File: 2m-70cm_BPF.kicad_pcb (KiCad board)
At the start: 2 copper layers, 68.2 x 24 mm, 18 parts, among them J1 Conn_Coaxial, J2 Conn_Coaxial

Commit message: Adjusted dividers masks.
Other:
- board text added: "3-POLE CHEBYSHEV BAND-PASS FILTER R1 Max. 37dBM - 5W"
- board text removed: "3-POLE CHEBYSHEV BAND-PASS FILTER R1"
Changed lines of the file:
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@@
 		(layer "Edge.Cuts")
 	)
-	(gr_text "3-POLE CHEBYSHEV \nBAND-PASS FILTER R1"
-		(at 126 129 0)
+	(gr_text "3-POLE CHEBYSHEV \nBAND-PASS FILTER R1\nMax. 37dBM - 5W"
+		(at 125.1 129.8 0)
 		(layer "F.Mask")
 		(effects
@@
 			)
 		)
+	)
+	(zone
+		(net 0)
+		(net_name "")
+		(layer "B.Mask")
+		(hatch edge 0.5)
+		(connect_pads yes
+			(clearance 0.3)
+		)
+		(min_thickness 0.25)
+		(filled_areas_thickness no)
+		(fill yes
+			(thermal_gap 0.5)
+			(thermal_bridge_width 0.5)
+		)
+		(polygon
+			(pts
+				(xy 109.3 132.5) (xy 107.7 132.2) (xy 109.5 123.6) (xy 111.1 123.9)
+			)
+		)
+	)
+	(zone
+		(net 0)
+		(net_name "")
+		(layer "B.Mask")
+		(hatch edge 0.5)
+		(connect_pads yes
+			(clearance 0.3)
+		)
+		(min_thickness 0.25)
+		(filled_areas_thickness no)
+		(fill yes
+			(thermal_gap 0.5)
+			(thermal_bridge_width 0.5)
+		)
+		(polygon
+			(pts
+				(xy 123.600001 147.9) (xy 121.989736 147.9) (xy 121.989737 123.9) (xy 123.6 123.9)
+			)
+		)
+	)
+	(zone
+		(net 0)
+		(net_name "")
+		(layer "B.Mask")
+		(hatch edge 0.5)
+		(connect_pads yes
+			(clearance 0.3)
+		)
+		(min_thickness 0.25)
+		(filled_areas_thickness no)
+		(fill yes
+			(thermal_gap 0.5)
+			(thermal_bridge_width 0.5)
+		)
+		(polygon
+			(pts
+				(xy 107.7 132.2) (xy 109.3 132.5) (xy 106.4 134.7) (xy 104.8 134.4)
+			)
+		)
+	)
+	(zone
+		(net 0)
+		(net_name "")
+		(layer "B.Mask")
+		(hatch edge 0.5)
+		(connect_pads yes
+			(clearance 0.3)
+		)
+		(min_thickness 0.25)
+		(filled_areas_thickness no)
+		(fill yes
+			(thermal_gap 0.5)
+			(thermal_bridge_width 0.5)
+		)
+		(polygon
+			(pts
+				(xy 104.5 148.3) (xy 102.9 147.9) (xy 104.8 134.4) (xy 106.4 134.7)
+			)
+		)

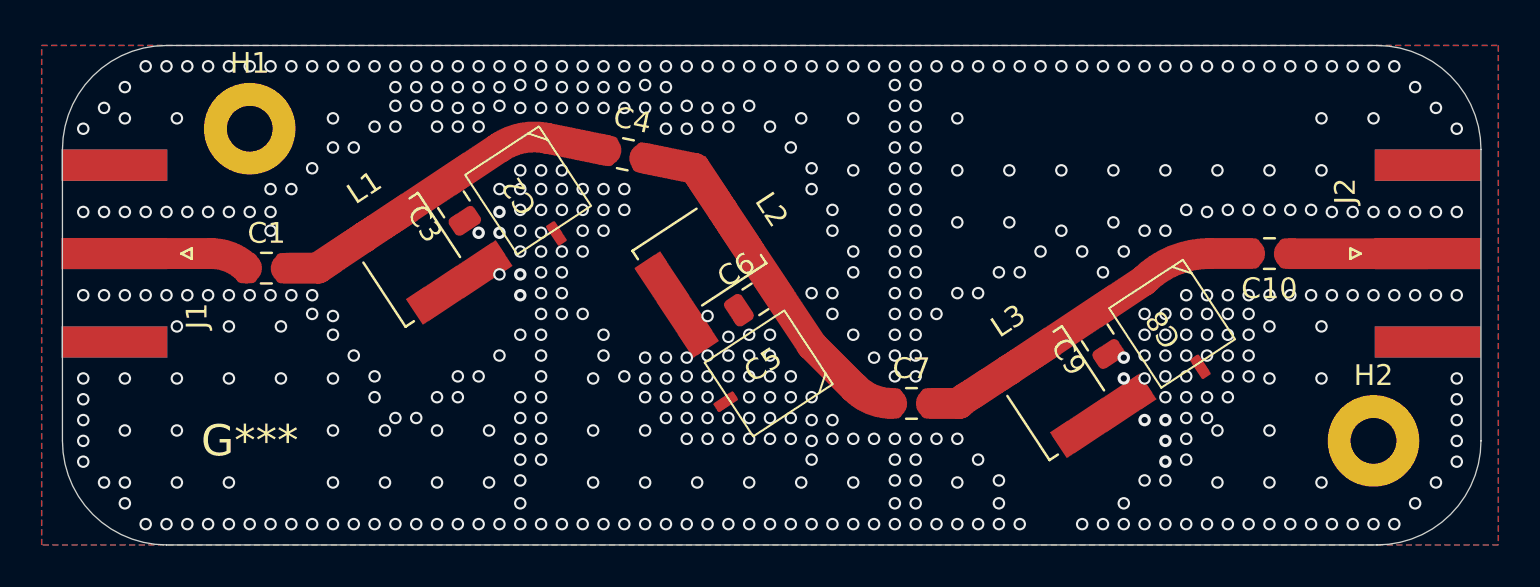
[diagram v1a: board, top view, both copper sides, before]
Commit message: Inductors changes to 35n5. Better Q, 2m-137MHz combo.
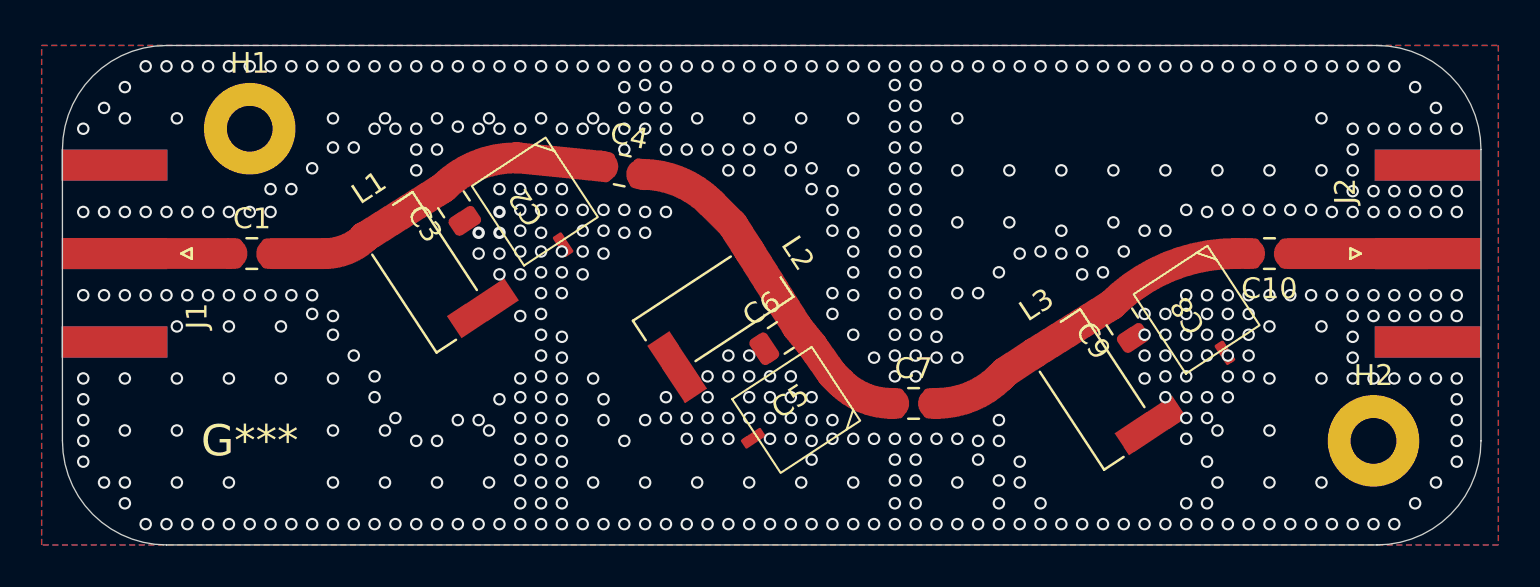
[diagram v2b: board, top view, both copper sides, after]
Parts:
- C3, C9: value 18p/200V -> 22p/200V
- C6: value 22p/200V -> 33p/200V
- L1, L2, L3: value 33n -> 35n5; footprint riske:L_Wurth_WE-CAIR-4248 -> riske:L_Wurth_WE-CAIR-3168
- moved L2 2.57 mm to (113.3, 136.7), turned to -56.699 degrees
- moved C6 2.22 mm to (116.5, 138.1)
- moved C5 2.19 mm to (117.3, 141.5)
- moved L3 1.76 mm to (131.5, 140.5)
- moved C9 1.41 mm to (132.9, 137.3)
- moved C8 1.36 mm to (136.5, 136.7)
- moved C1 0.99 mm to (91.1, 134.0)
- moved L1 0.86 mm to (99.4, 134.9)
- moved C4 0.79 mm to (108.9, 130.0), turned to -11.5 degrees
- moved C2 0.63 mm to (104.7, 131.5)
- moved C7 0.10 mm to (122.9, 141.2)
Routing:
- net Net-(J1-In): track 6.53 -> 5.65 mm
- net GND: vias 519 -> 541
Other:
- board text added: "3-POLE CHEBYSHEV BAND-PASS FILTER R1"
- board text added: "Max. 37dBM - 5W"
- board text removed: "3-POLE CHEBYSHEV BAND-PASS FILTER R1 Max. 37dBM - 5W"
